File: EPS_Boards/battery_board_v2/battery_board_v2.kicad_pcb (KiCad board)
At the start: 4 copper layers, 90.2 x 96 mm, 122 parts, among them J1 PC104_Connector, J2 Programming Header, J3 System Test Connector, J4 Conn_01x08_Male, J5 RBF, J6 RBF Deployment Bypass, J7 30s Timer, J8 Shunt Resistor, Q1 CSD16401Q5, Q10 CSD16401Q5, Q11 NTJD1155LT1G, Q2 CSD16401Q5, Q3 CSD16401Q5, Q4 CSD16401Q5, Q5 CSD16401Q5, Q6 CSD16401Q5, Q7 CSD16401Q5, Q8 CSD16401Q5, Q9 CSD16401Q5, U1 TMP36xS, U10 BQ297xx, U11 BQ297xx, U12 INA219AxD, U13 TPS24750, U2 STM32F030F4Px, U3 TPS63000-Q1, U4 LTC6995HS6-1#TRMPBF, U5 LTC6995HS6-1#TRMPBF, U6 74AUP1G08, U7 UCC2946D, U8 BQ297xx, U9 BQ297xx, Y1 16 MHz

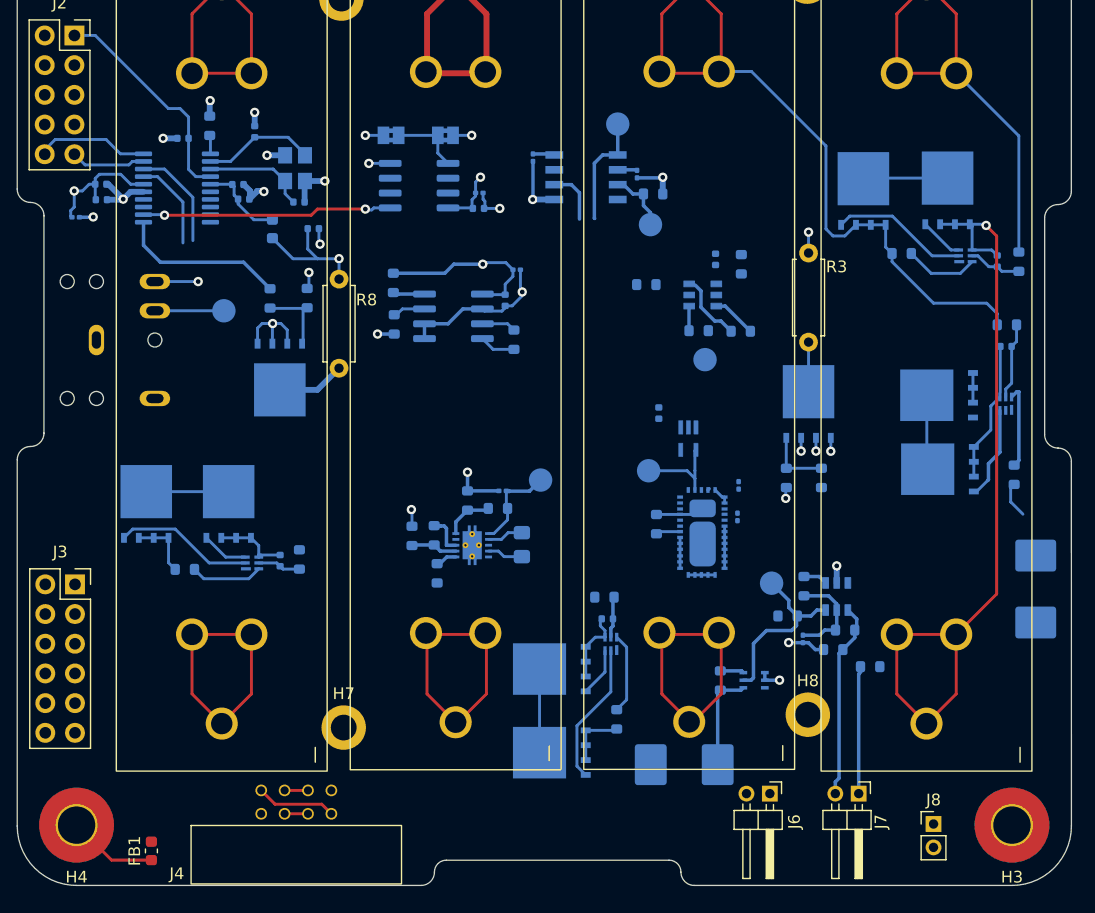
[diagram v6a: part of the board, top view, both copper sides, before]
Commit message: eps: battery board: more traces
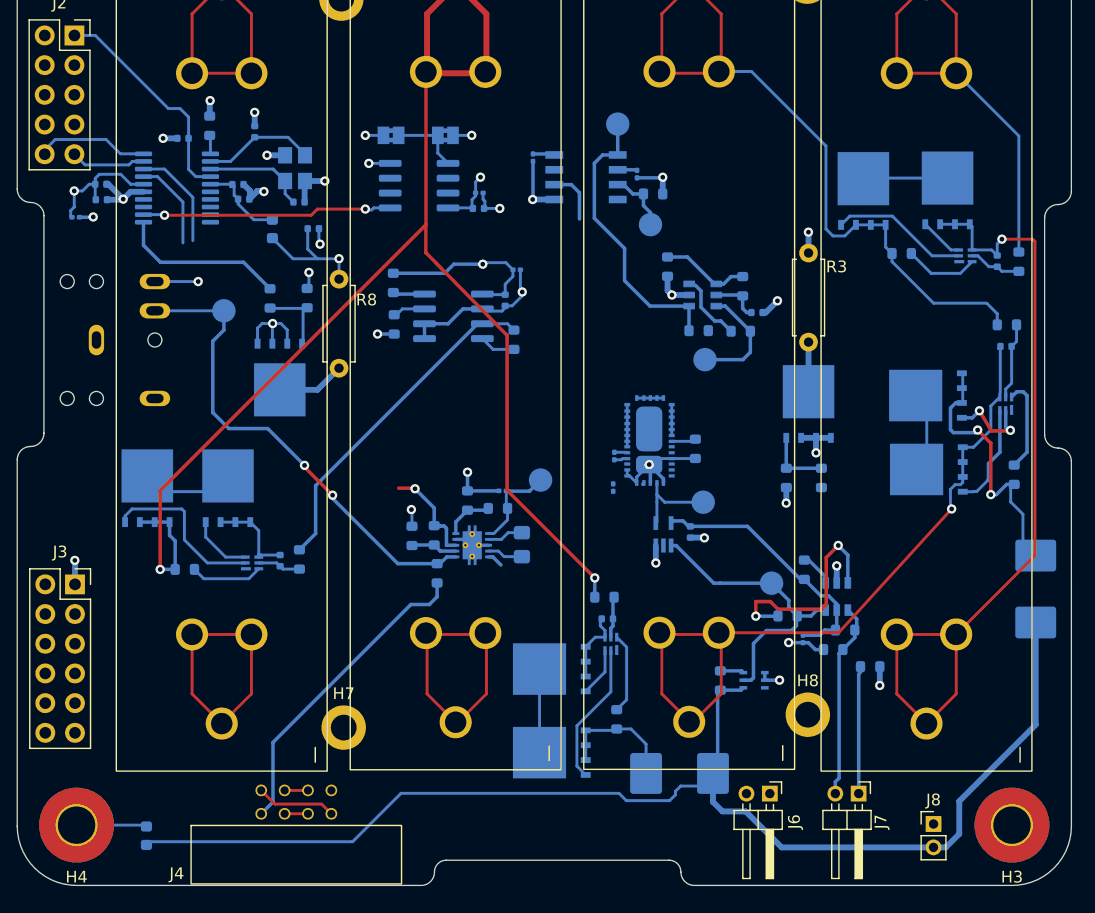
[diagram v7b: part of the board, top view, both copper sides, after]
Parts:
- FB1: moved to B.Cu
- moved C21 11.7 mm to (160.3, 106.2), turned to -90 degrees
- moved C22 10.7 mm to (160.2, 108.9), turned to 90 degrees
- moved C14 10.5 mm to (166.8, 112.7), turned to 90 degrees
- moved U13 9.39 mm to (163.5, 104.6), turned to 90 degrees
- moved U6 8.46 mm to (164.5, 112.9), turned to 90 degrees
- moved R37 7.25 mm to (167.2, 105.6), turned to -90 degrees
- moved C11 5.77 mm to (172.5, 94.0), turned to 0 degrees
- moved TP6 5.39 mm to (167.9, 110.2), turned to 0 degrees
- moved R12 2.38 mm to (164.8, 90.0), turned to -90 degrees
- moved R11 1.88 mm to (171.3, 91.7)
- moved R18 1.41 mm to (176.6, 116.0)
- moved FB1 1.37 mm to (120.3, 138.7), turned to -90 degrees
- moved Q5 1.35 mm to (120.3, 109.0)
- moved Q3 1.35 mm to (127.2, 109.0)
- moved Q9 0.95 mm to (187.2, 107.4)
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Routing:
- net PACK_N: track 8.52 -> 106.6 mm
- net Net-(B2-Pad1): track 27.9 -> 120.3 mm, vias 0 -> 2
- net Net-(J5-Pad4): track 7.74 -> 41.6 mm, vias 0 -> 2
- net Net-(B3-Pad2): track 34.5 -> 63.2 mm, vias 0 -> 1
- net Net-(J4-Pad8): track 0.00 -> 26.9 mm
- net IV_MON_N: track 128.8 -> 154.9 mm
- net GND: track 94.7 -> 113.8 mm, vias 27 -> 31
- net Net-(R22-Pad2): track 0.00 -> 18.6 mm, vias 0 -> 2
- net 3V3_CON: track 16.3 -> 34.9 mm
- net Net-(F2-Pad1): track 5.65 -> 23.5 mm, vias 0 -> 2
- net nRST_HB: track 11.8 -> 24.6 mm
- net EN_D3: track 15.4 -> 25.3 mm
- net Net-(R11-Pad2): track 0.00 -> 7.64 mm
- net Net-(Q7-Pad4): track 0.25 -> 7.17 mm, vias 0 -> 2
- net Net-(J6-Pad1): track 3.39 -> 10.00 mm, vias 0 -> 1
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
